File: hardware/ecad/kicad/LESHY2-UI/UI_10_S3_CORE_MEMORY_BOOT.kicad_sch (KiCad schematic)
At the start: 33 parts, among them J10001 GCT RFPC-SMA32-FN-175-A, J10002 Hirose U.FL-R-SMT-1(10), J10003 Samtec FTSH-105-01-L-DV-K-P-TR, SW10001 Alps Alpine SKRTLAE010, SW10002 Alps Alpine SKRTLAE010, U10001 ESP32-S3-WROOM-1U-N16R8, U10002 KYOCERA AVX CP0603Q5425ENTR, U10003 Texas Instruments TPD4E05U06D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, U10004 Murata GRM21BR60J226ME39L, X10001 ESP32-S3-WROOM-1U-N16R8 facto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

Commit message: Optimize H1 display and stocked BOM routes
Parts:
- C10003, C10004: value TDK C1005X7R1H104K050BB -> Yageo CC0402KRX7R9BB104
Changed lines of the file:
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@@
 			(effects (font (size 1.27 1.27)))
 		)
-		(property "Value" "TDK C1005X7R1H104K050BB"
+		(property "Value" "Yageo CC0402KRX7R9BB104"
 			(at 335.28 110.49 0)
 			(show_name no)
@@
 			(effects (font (size 1.27 1.27)))
 		)
-		(property "Value" "TDK C1005X7R1H104K050BB"
+		(property "Value" "Yageo CC0402KRX7R9BB104"
 			(at 243.84 222.25 0)
 			(show_name no)

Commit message: Replace six pre-order resistor identities
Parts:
- R10006, R10007: value Yageo RC0402FR-072K2L -> UNI-ROYAL 0402WGF2201TCE
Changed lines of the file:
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@@
 			(effects (font (size 1.27 1.27)))
 		)
-		(property "Value" "Yageo RC0402FR-072K2L"
+		(property "Value" "UNI-ROYAL 0402WGF2201TCE"
 			(at 60.96 133.35 0)
 			(show_name no)
@@
 			(effects (font (size 1.27 1.27)))
 		)
-		(property "Value" "Yageo RC0402FR-072K2L"
+		(property "Value" "UNI-ROYAL 0402WGF2201TCE"
 			(at 243.84 138.43 0)
 			(show_name no)

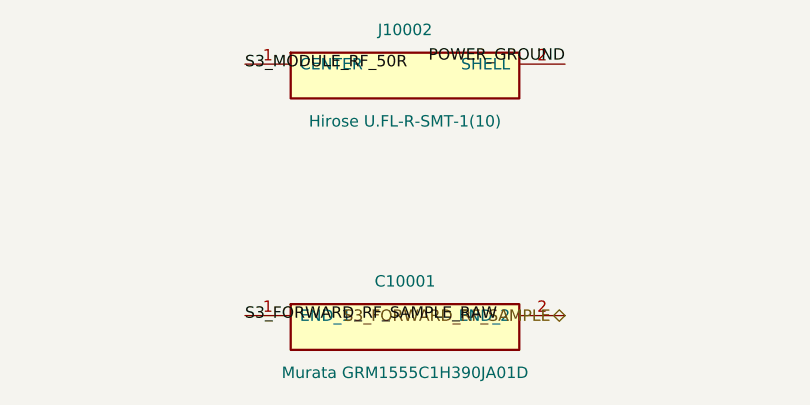
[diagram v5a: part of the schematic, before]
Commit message: Audit top 20 costs and accept stocked U.FL route
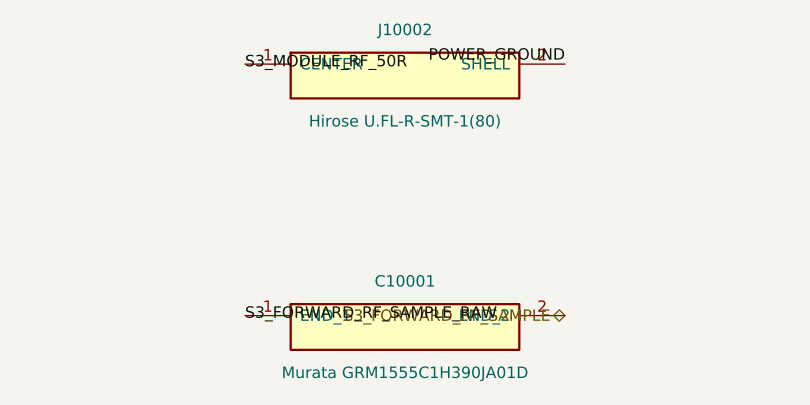
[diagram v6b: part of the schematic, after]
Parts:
- J10002: value Hirose U.FL-R-SMT-1(10) -> Hirose U.FL-R-SMT-1(80)
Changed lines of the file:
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@@
 			(effects (font (size 1.27 1.27)))
 		)
-		(property "Value" "Hirose U.FL-R-SMT-1(10)"
+		(property "Value" "Hirose U.FL-R-SMT-1(80)"
 			(at 335.28 54.61 0)
 			(show_name no)
